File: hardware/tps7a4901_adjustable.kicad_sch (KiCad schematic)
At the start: 9 parts, among them U8 TPS7A4901DGNR

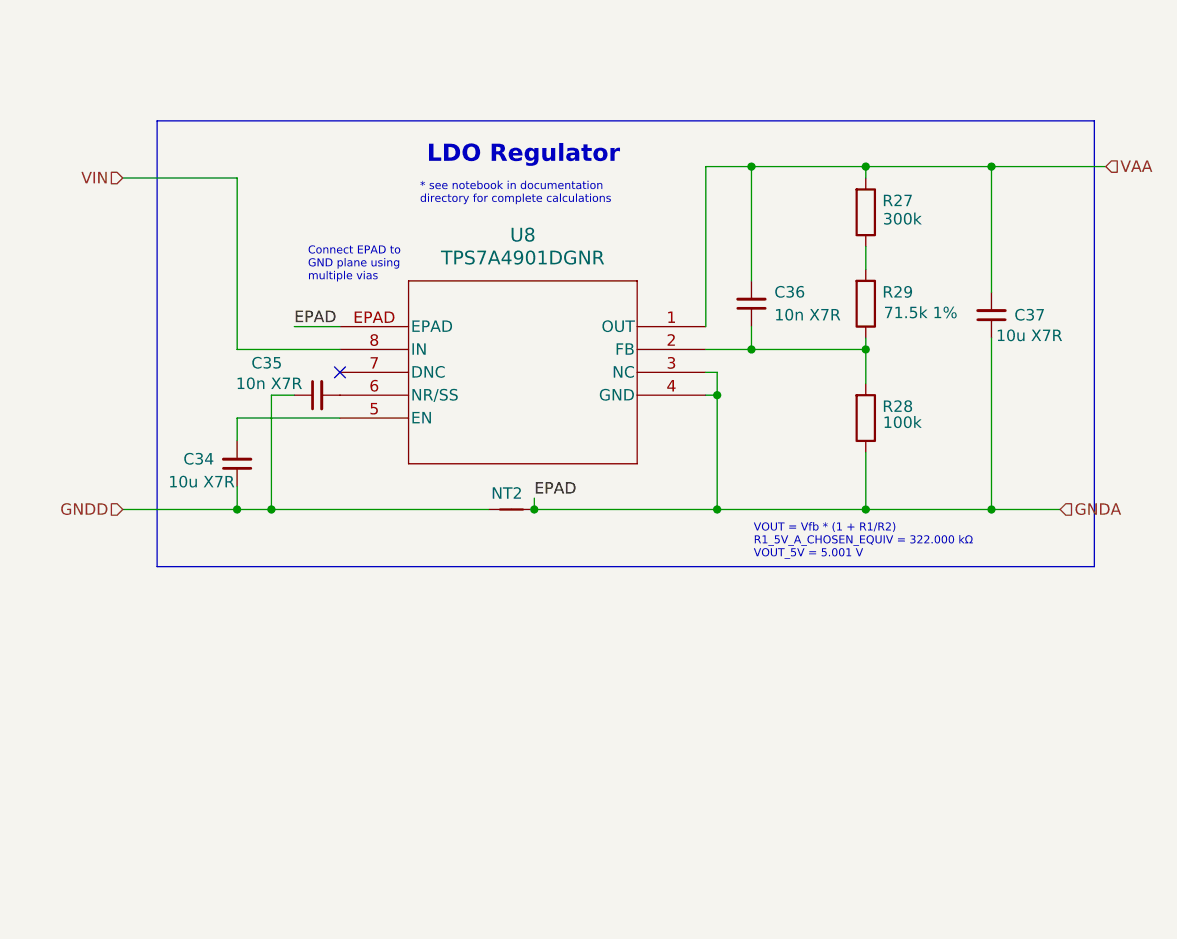
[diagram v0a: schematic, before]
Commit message: finalize board before switch to stm
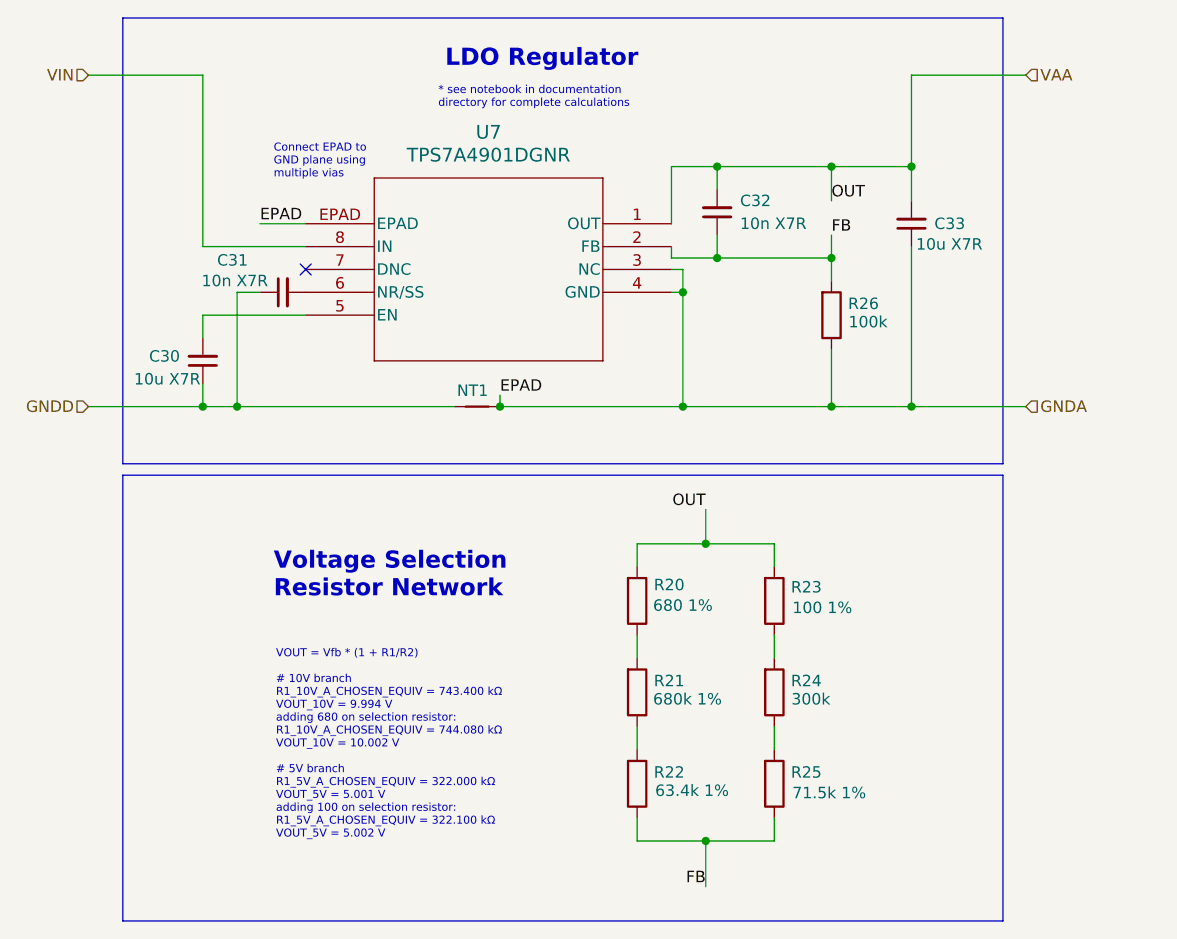
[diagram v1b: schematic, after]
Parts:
- removed C34, C37: 10u X7R, Capacitor_SMD:C_1206_3216Metric, symbol Device:C_Small
- removed C35, C36: 10n X7R, Capacitor_SMD:C_1206_3216Metric, symbol Device:C_Small
- removed NT2: NetTie_2, NetTie:NetTie-2_SMD_Pad2.0mm, symbol Device:NetTie_2
- removed R27: 300k, symbol Device:R
- removed R28: 100k, symbol Device:R
- removed R29: 71.5k 1%, symbol Device:R
- removed U8: TPS7A4901DGNR, kml-custom:DGN8_1P89X1P57, symbol kml-custom:TPS7A4901DGNR
- added C30, C33: 10u X7R, Capacitor_SMD:C_1206_3216Metric, symbol Device:C_Small
- added C31, C32: 10n X7R, Capacitor_SMD:C_1206_3216Metric, symbol Device:C_Small
- added NT1: NetTie_2, NetTie:NetTie-2_SMD_Pad2.0mm, symbol Device:NetTie_2
- added R20: 680 1%, symbol Device:R
- added R21: 680k 1%, symbol Device:R
- added R22: 63.4k 1%, symbol Device:R
- added R23: 100 1%, symbol Device:R
- added R24: 300k, symbol Device:R
- added R25: 71.5k 1%, symbol Device:R
- added R26: 100k, symbol Device:R
- added U7: TPS7A4901DGNR, kml-custom:DGN8_1P89X1P57, symbol kml-custom:TPS7A4901DGNR
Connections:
- net GNDA: now also C33.1, NT1.2, R26.1, U7.3 (NC), U7.4 (GND), U7.EPAD
- net GNDD: now also C30.1, C31.1, NT1.1
- net VAA: now also C32.2, C33.2, R20.2, R23.2, U7.1 (OUT)
- net VIN: now also U7.8 (IN)
- new net: R24.1, R25.2
- new net: R23.1, R24.2
- new net: R20.1, R21.2
- new net: C30.2, U7.5 (EN)
- new net: R21.1, R22.2
- new net: C31.2, U7.6 (NR/SS)
- new net FB: C32.1, R22.1, R25.1, R26.2, U7.2 (FB)
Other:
- note added: "VOUT = Vfb * (1 + R1/R2) # 10V branch R1_10V_A_CHOSEN_EQUIV = 743.400 kΩ VOUT_10V = 9.994 V adding 680 on selection resistor: R1_10V_A_CHOSEN_EQUIV = 744.080 kΩ VOUT_10V = 10.002 V # 5V branch R1_5V_A_CHOSEN_EQUIV = 322.000 kΩ VOUT_5V = 5.001 V adding 100 on selection resistor: R1_5V_A_CHOSEN_EQUIV = 322.100 kΩ VOUT_5V = 5.002 V"
- note added: "Voltage Selection Resistor Network"
- note removed: "VOUT = Vfb * (1 + R1/R2) R1_5V_A_CHOSEN_EQUIV = 322.000 kΩ VOUT_5V = 5.001 V"

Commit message: final iteration of board with proper connectors and clean layout
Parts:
- C32: renamed from C30; footprint Capacitor_SMD:C_1206_3216Metric -> Capacitor_SMD:C_1206_3216Metric_Pad1.33x1.80mm_HandSolder
- C33: renamed from C31; footprint Capacitor_SMD:C_1206_3216Metric -> Capacitor_SMD:C_0603_1608Metric_Pad1.08x0.95mm_HandSolder
- C34: renamed from C32; footprint Capacitor_SMD:C_1206_3216Metric -> Capacitor_SMD:C_0603_1608Metric_Pad1.08x0.95mm_HandSolder
- C35: renamed from C33; footprint Capacitor_SMD:C_1206_3216Metric -> Capacitor_SMD:C_1206_3216Metric_Pad1.33x1.80mm_HandSolder
- R21: renamed from R20; footprint (none) -> Resistor_SMD:R_0805_2012Metric_Pad1.20x1.40mm_HandSolder
- R22: renamed from R21; footprint (none) -> Resistor_SMD:R_0805_2012Metric_Pad1.20x1.40mm_HandSolder
- R23: renamed from R22; footprint (none) -> Resistor_SMD:R_0805_2012Metric_Pad1.20x1.40mm_HandSolder
- R24: renamed from R23; footprint (none) -> Resistor_SMD:R_0805_2012Metric_Pad1.20x1.40mm_HandSolder
- R25: renamed from R24; value 300k -> 300k 1%; footprint (none) -> Resistor_SMD:R_0805_2012Metric_Pad1.20x1.40mm_HandSolder
- R26: renamed from R25; footprint (none) -> Resistor_SMD:R_0805_2012Metric_Pad1.20x1.40mm_HandSolder
- R27: renamed from R26; value 100k -> 100k 1%; footprint (none) -> Resistor_SMD:R_0805_2012Metric_Pad1.20x1.40mm_HandSolder
- renumbered NT1 to NT2, U7 to U8
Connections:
- net VIN: now also C32.2, U8.5 (EN)
- net GNDD renamed GND
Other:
- note added: "10V branch"
- note added: "5V branch"
- moved on the sheet: C32
